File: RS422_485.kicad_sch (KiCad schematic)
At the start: 10 parts, among them U1101 THVD1424

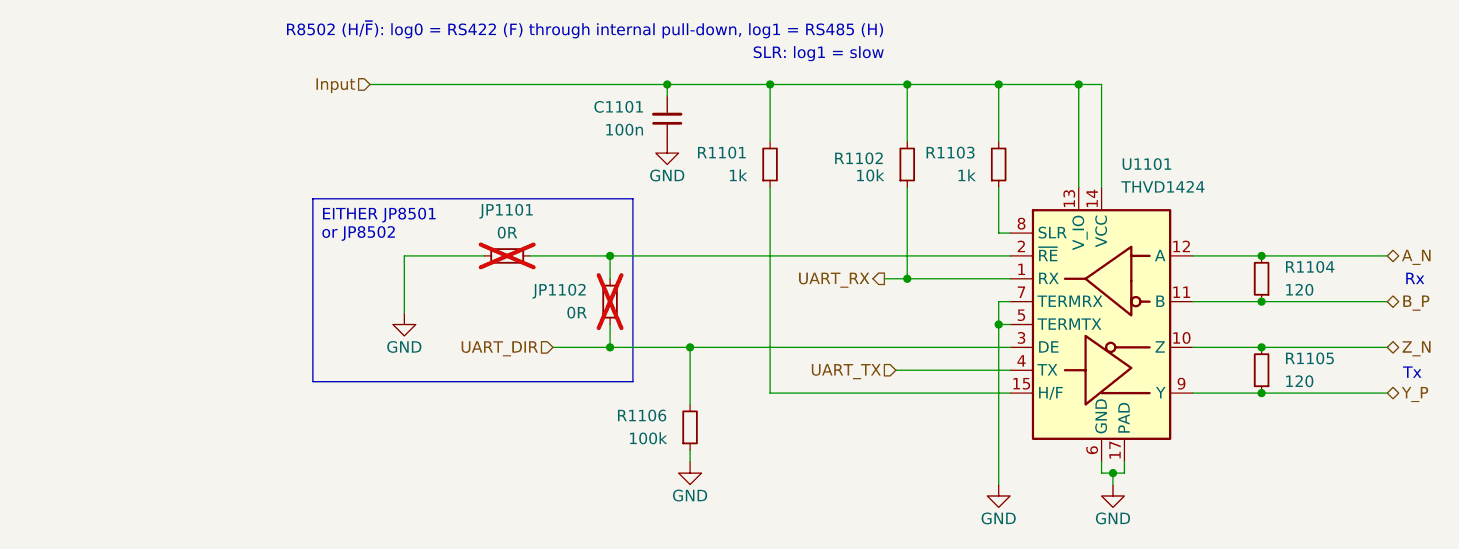
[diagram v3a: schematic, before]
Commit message: pcb progres for all components
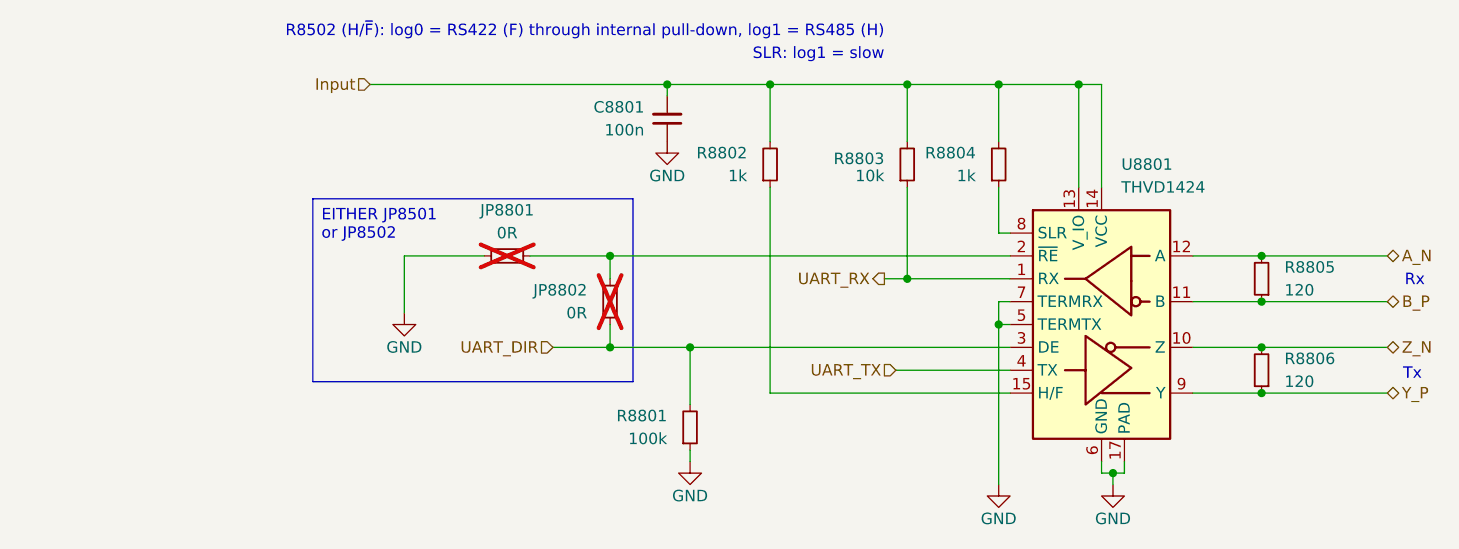
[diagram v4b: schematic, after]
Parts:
- renumbered C1101 to C8801, JP1101 to JP8801, JP1102 to JP8802, R1106 to R8801, R1101 to R8802, R1102 to R8803, R1103 to R8804, R1104 to R8805, R1105 to R8806, U1101 to U8801
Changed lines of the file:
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@@
 		(on_board yes)
 		(dnp no)
-		(property "Reference" "R1104"
+		(property "Reference" "R8805"
 			(at 208.28 97.7899 0)
 			(effects
@@
 		(on_board yes)
 		(dnp no)
-		(property "Reference" "R1102"
+		(property "Reference" "R8803"
 			(at 163.83 85.725 0)
 			(effects
@@
 		(dnp yes)
 		(fields_autoplaced yes)
-		(property "Reference" "JP1101"
+		(property "Reference" "JP8801"
 			(at 121.92 91.44 90)
 			(effects
@@
 		(on_board yes)
 		(dnp no)
-		(property "Reference" "#PWR0328"
+		(property "Reference" "#PWR08803"
 			(at 142.24 125.73 0)
 			(effects
@@
 		(dnp no)
 		(fields_autoplaced yes)
-		(property "Reference" "C1101"
+		(property "Reference" "C8801"
 			(at 137.16 80.0035 0)
 			(effects
@@
 		(dnp no)
 		(fields_autoplaced yes)
-		(property "Reference" "R1101"
+		(property "Reference" "R8802"
 			(at 148.59 85.09 0)
 			(effects
@@
 		(on_board yes)
 		(dnp no)
-		(property "Reference" "#PWR0324"
+		(property "Reference" "#PWR08805"
 			(at 189.23 128.27 0)
 			(effects
@@
 		(dnp no)
 		(fields_autoplaced yes)
-		(property "Reference" "R1103"
+		(property "Reference" "R8804"
 			(at 173.99 85.09 0)
 			(effects
@@
 		(on_board yes)
 		(dnp no)
-		(property "Reference" "#PWR0327"
+		(property "Reference" "#PWR08801"
 			(at 110.49 109.22 0)
 			(effects
@@
 		(dnp no)
 		(fields_autoplaced yes)
-		(property "Reference" "R1106"
+		(property "Reference" "R8801"
 			(at 139.7 114.2999 0)
 			(effects
@@
 		(dnp no)
 		(fields_autoplaced yes)
-		(property "Reference" "U1101"
+		(property "Reference" "U8801"
 			(at 190.1541 86.36 0)
 			(effects
@@
 		(on_board yes)
 		(dnp no)
-		(property "Reference" "#PWR0325"
+		(property "Reference" "#PWR08804"
 			(at 176.53 128.27 0)
 			(effects
@@
 		(on_board yes)
 		(dnp no)
-		(property "Reference" "R1105"
+		(property "Reference" "R8806"
 			(at 208.28 107.9499 0)
 			(effects
@@
 		(on_board yes)
 		(dnp no)
-		(property "Reference" "#PWR0326"
+		(property "Reference" "#PWR08802"
 			(at 139.7 90.17 0)
 			(effects
@@
 		(dnp yes)
 		(fields_autoplaced yes)
-		(property "Reference" "JP1102"
+		(property "Reference" "JP8802"
 			(at 130.81 100.33 0)
 			(effects
